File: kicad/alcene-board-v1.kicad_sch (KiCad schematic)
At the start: 8 parts, among them J1 ESP32-S3-DevKitC-1_J1, J2 USB-C Input, J3 ESP32-S3-DevKitC-1_J3, J4 ILI9341_TFT_14pin

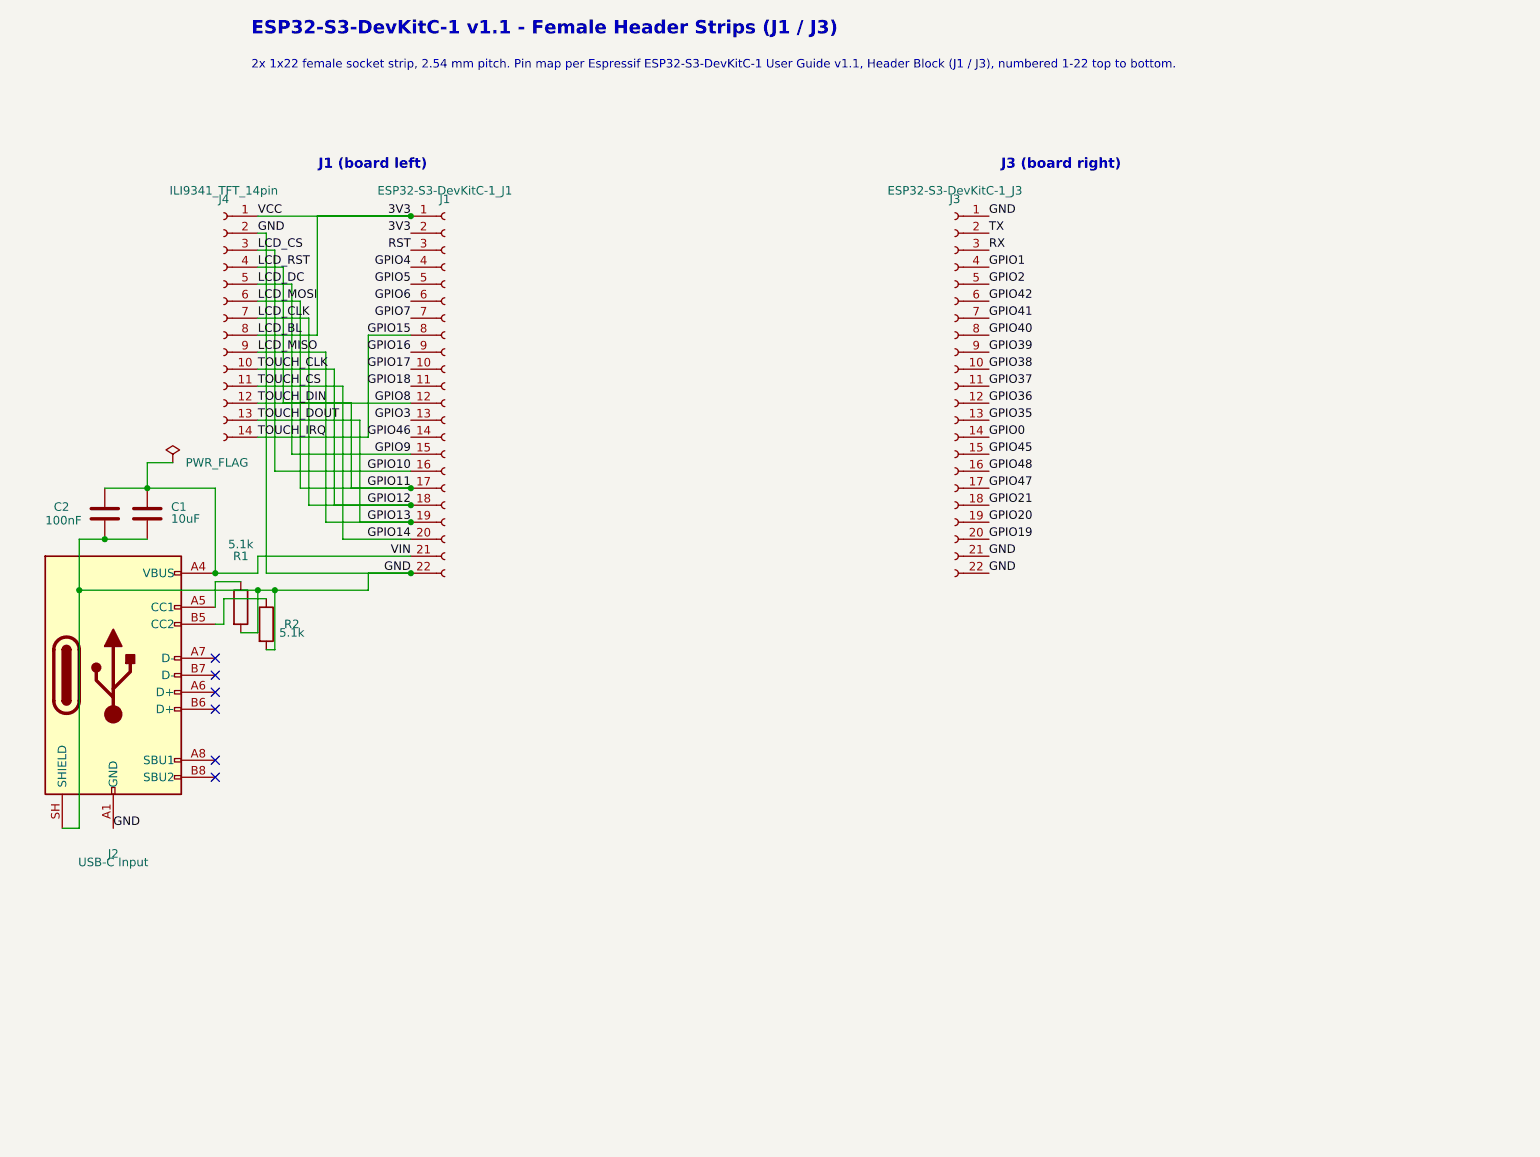
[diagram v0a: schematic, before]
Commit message: feat: tidy up TFT to ESP32 connection
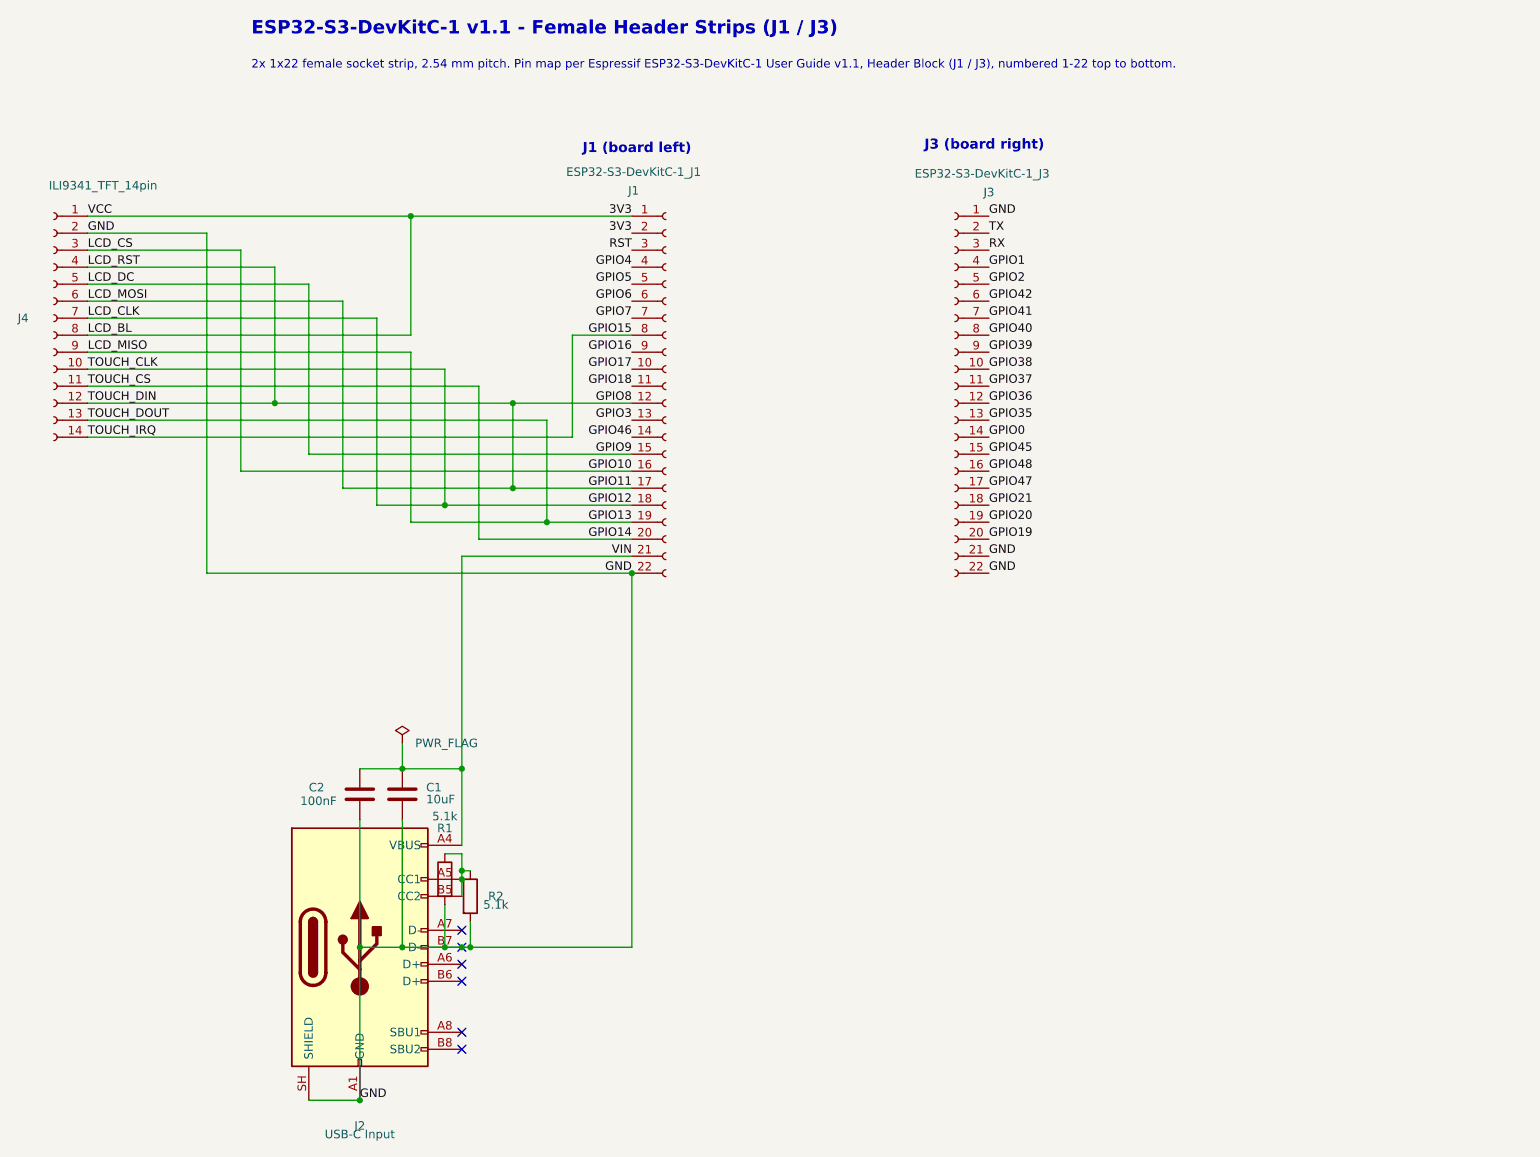
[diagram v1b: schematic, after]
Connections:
- net GND: now also J2.B7 (D-)
- net at J2.B5 (CC2), R2.1: now also J2.A5 (CC1), R1.1
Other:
- moved on the sheet: C1, C2, J1, J2, J4, R1, R2

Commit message: feat: USB type C schema tidy up
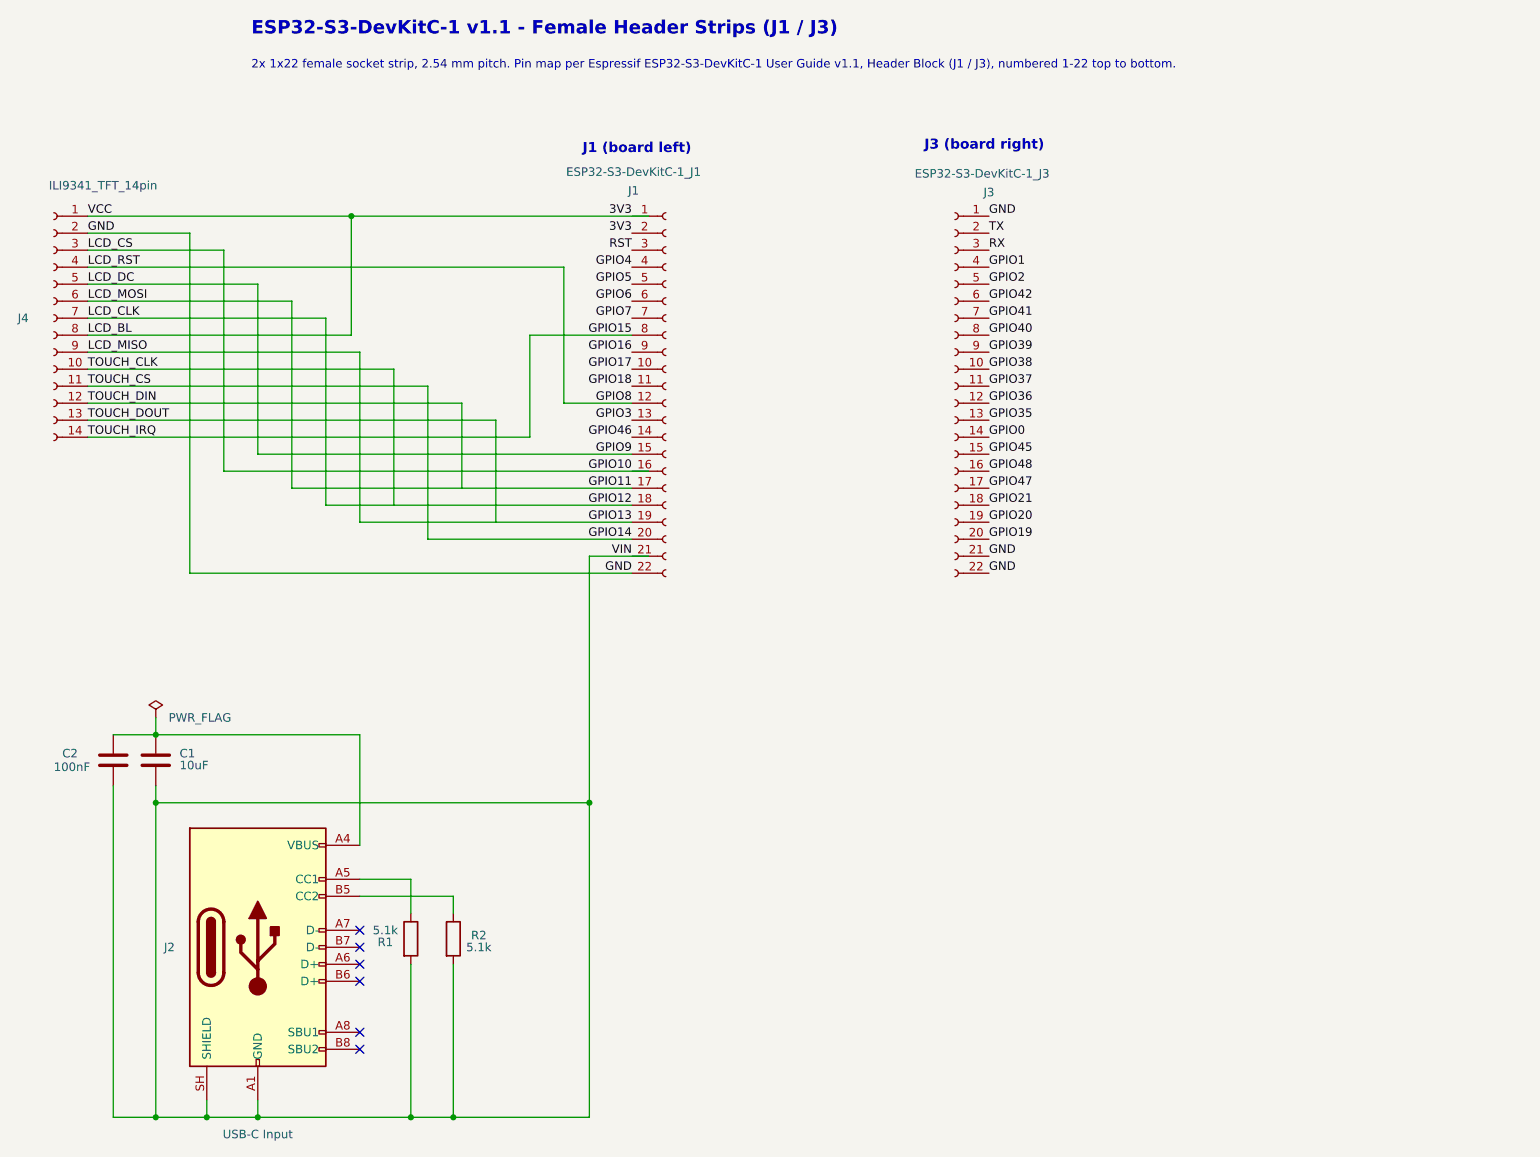
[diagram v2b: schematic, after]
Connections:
- net GND: no longer C1.2, C2.2, J2.A1 (GND), J2.A12 (GND), J2.B1 (GND), J2.B12 (GND), J2.B7 (D-), J2.SH (SHIELD), R1.2, R2.2
- net GPIO11: no longer J1.12 (Pin_12), J4.12 (Pin_12), J4.4 (Pin_4)
- net GPIO12: no longer J4.10 (Pin_10)
- net GPIO13: no longer J4.13 (Pin_13)
- net VIN: now also C1.2, C2.2, J2.A1 (GND), J2.A12 (GND), J2.B1 (GND), J2.B12 (GND), J2.SH (SHIELD), R1.2, R2.2; no longer C1.1, C2.1, J2.A4 (VBUS), J2.A9 (VBUS), J2.B4 (VBUS), J2.B9 (VBUS)
- net at J2.B5 (CC2), R2.1: no longer J2.A5 (CC1), R1.1
- new net: C1.1, C2.1, J2.A4 (VBUS), J2.A9 (VBUS), J2.B4 (VBUS), J2.B9 (VBUS)
- new net: J2.A5 (CC1), R1.1
- new net GPIO8: J1.12 (Pin_12), J4.4 (Pin_4)
- new net TOUCH_CLK: J4.10 (Pin_10)
- new net TOUCH_DIN: J4.12 (Pin_12)
- new net TOUCH_DOUT: J4.13 (Pin_13)
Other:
- moved on the sheet: C1, C2, J2, R1, R2

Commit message: feat: type C wiring fix
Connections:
- net VIN: now also C1.1, C2.1, J2.A4 (VBUS), J2.A9 (VBUS), J2.B4 (VBUS), J2.B9 (VBUS); no longer C1.2, C2.2, J2.A1 (GND), J2.A12 (GND), J2.B1 (GND), J2.B12 (GND), J2.SH (SHIELD), R1.2, R2.2
- new net: C1.2, C2.2, J2.A1 (GND), J2.A12 (GND), J2.B1 (GND), J2.B12 (GND), J2.SH (SHIELD), R1.2, R2.2
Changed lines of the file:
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@@
-	)
-	(junction
-		(at 110.49 138.43)
-		(diameter 0)
-		(color 0 0 0 0)
 	)
 	(junction
@@
 	)
 	(junction
-		(at 45.72 138.43)
-		(diameter 0)
-		(color 0 0 0 0)
-	)
-	(junction
 		(at 45.72 128.27)
 		(diameter 0)
 		(color 0 0 0 0)
 	)
+	(junction
+		(at 76.2 144.78)
+		(diameter 0)
+		(color 0 0 0 0)
+	)
 	(no_connect
 		(at 76.2 160.02)
@@
 	(wire
 		(pts
+			(xy 76.2 144.78) (xy 101.6 144.78)
+		)
+		(stroke
+			(width 0)
+			(type default)
+		)
+	)
+	(wire
+		(pts
 			(xy 35.56 81.28) (xy 96.52 81.28)
 		)
@@
 	(wire
 		(pts
-			(xy 60.96 185.42) (xy 83.82 185.42)
+			(xy 60.96 185.42) (xy 106.68 185.42)
 		)
 		(stroke
@@
 	(wire
 		(pts
-			(xy 90.17 185.42) (xy 110.49 185.42)
-		)
-		(stroke
-			(width 0)
-			(type default)
-		)
-	)
-	(wire
-		(pts
 			(xy 35.56 55.88) (xy 55.88 55.88)
 		)
@@
 	(wire
 		(pts
-			(xy 110.49 101.6) (xy 110.49 185.42)
+			(xy 101.6 101.6) (xy 116.84 101.6)
+		)
+		(stroke
+			(width 0)
+			(type default)
+		)
+	)
+	(wire
+		(pts
+			(xy 101.6 144.78) (xy 101.6 101.6)
 		)
 		(stroke
@@
 	(wire
 		(pts
-			(xy 45.72 138.43) (xy 45.72 185.42)
-		)
-		(stroke
-			(width 0)
-			(type default)
-		)
-	)
-	(wire
-		(pts
 			(xy 35.56 76.2) (xy 86.36 76.2)
 		)
@@
 	(wire
 		(pts
+			(xy 106.68 185.42) (xy 106.68 104.14)
+		)
+		(stroke
+			(width 0)
+			(type default)
+		)
+	)
+	(wire
+		(pts
 			(xy 55.88 55.88) (xy 55.88 88.9)
 		)
@@
 	(wire
 		(pts
-			(xy 110.49 101.6) (xy 119.38 101.6)
-		)
-		(stroke
-			(width 0)
-			(type default)
-		)
-	)
-	(wire
-		(pts
-			(xy 83.82 185.42) (xy 90.17 185.42)
-		)
-		(stroke
-			(width 0)
-			(type default)
-		)
-	)
-	(wire
-		(pts
-			(xy 45.72 138.43) (xy 110.49 138.43)
-		)
-		(stroke
-			(width 0)
-			(type default)
-		)
-	)
-	(wire
-		(pts
 			(xy 101.6 68.58) (xy 116.84 68.58)
 		)
@@
 	(wire
 		(pts
-			(xy 45.72 135.89) (xy 45.72 138.43)
-		)
-		(stroke
+			(xy 45.72 135.89) (xy 45.72 185.42)
+		)
+		(stroke

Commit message: feat: Alcene Board V1 final USB type C and TFT
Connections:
- net TOUCH_CLK is gone; now on net GPIO12: J4.10 (Pin_10)
- net TOUCH_DIN is gone; now on net GPIO11: J4.12 (Pin_12)
- net TOUCH_DOUT is gone; now on net GPIO13: J4.13 (Pin_13)
- net GND: now also C1.2, C2.2, J2.A1 (GND), J2.A12 (GND), J2.B1 (GND), J2.B12 (GND), J2.SH (SHIELD), R1.2, R2.2
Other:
- note added: "Alcene Board V1 - ESP32 S3 Centric Board"
- note added: "Espressif's ESP32-S3-DevKitC-1 Layout with TFT Display and expansion board design."
- note removed: "2x 1x22 female socket strip, 2.54 mm pitch. Pin map per Espressif ESP32-S3-DevKitC-1 User Guide v1.1, Header Block (J1 / J3), numbered 1-22 top to bottom."
- note removed: "ESP32-S3-DevKitC-1 v1.1 - Female Header Strips (J1 / J3)"
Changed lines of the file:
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@@
 		)
 	)
-	(text "ESP32-S3-DevKitC-1 v1.1 - Female Header Strips (J1 / J3)"
+	(text "Alcene Board V1 - ESP32 S3 Centric Board"
 		(exclude_from_sim no)
 		(at 60 24 0)
@@
 		)
 	)
-	(text "2x 1x22 female socket strip, 2.54 mm pitch. Pin map per Espressif ESP32-S3-DevKitC-1 User Guide v1.1, Header Block (J1 / J3), numbered 1-22 top to bottom."
+	(text "Espressif's ESP32-S3-DevKitC-1 Layout with TFT Display and expansion board design."
 		(exclude_from_sim no)
 		(at 60 29 0)
@@
 	)
 	(junction
+		(at 81.28 93.98)
+		(diameter 0)
+		(color 0 0 0 0)
+	)
+	(junction
+		(at 91.44 91.44)
+		(diameter 0)
+		(color 0 0 0 0)
+	)
+	(junction
 		(at 53.34 185.42)
 		(diameter 0)
@@
 	)
 	(junction
+		(at 96.52 96.52)
+		(diameter 0)
+		(color 0 0 0 0)
+	)
+	(junction
+		(at 83.82 185.42)
+		(diameter 0)
+		(color 0 0 0 0)
+	)
+	(junction
+		(at 106.68 104.14)
+		(diameter 0)
+		(color 0 0 0 0)
+	)
+	(junction
+		(at 45.72 185.42)
+		(diameter 0)
+		(color 0 0 0 0)
+	)
+	(junction
+		(at 90.17 185.42)
+		(diameter 0)
+		(color 0 0 0 0)
+	)
+	(junction
+		(at 60.96 185.42)
+		(diameter 0)
+		(color 0 0 0 0)
+	)
+	(junction
 		(at 74.93 50.8)
-		(diameter 0)
-		(color 0 0 0 0)
-	)
-	(junction
-		(at 83.82 185.42)
-		(diameter 0)
-		(color 0 0 0 0)
-	)
-	(junction
-		(at 45.72 185.42)
-		(diameter 0)
-		(color 0 0 0 0)
-	)
-	(junction
-		(at 90.17 185.42)
-		(diameter 0)
-		(color 0 0 0 0)
-	)
-	(junction
-		(at 60.96 185.42)
 		(diameter 0)
 		(color 0 0 0 0)
@@
 	(wire
 		(pts
-			(xy 55.88 88.9) (xy 119.38 88.9)
-		)
-		(stroke
-			(width 0)
-			(type default)
-		)
-	)
-	(wire
-		(pts
 			(xy 91.44 78.74) (xy 91.44 91.44)
 		)
@@
 	(wire
 		(pts
+			(xy 55.88 88.9) (xy 116.84 88.9)
+		)
+		(stroke
+			(width 0)
+			(type default)
+		)
+	)
+	(wire
+		(pts
 			(xy 76.2 96.52) (xy 116.84 96.52)
 		)
@@
 	(wire
 		(pts
+			(xy 74.93 50.8) (xy 116.84 50.8)
+		)
+		(stroke
+			(width 0)
+			(type default)
+		)
+	)
+	(wire
+		(pts
 			(xy 74.93 68.58) (xy 74.93 50.8)
 		)
@@
 		)
 		(stroke
-			(width 0)
-			(type default)
-		)
-	)
-	(wire
-		(pts
-			(xy 74.93 50.8) (xy 119.38 50.8)
-		)
-		(stroke
